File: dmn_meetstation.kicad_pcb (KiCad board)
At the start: 2 copper layers, 19.1 x 80 mm, 19 parts, among them J1 USB_OTG, J2 Conn_01x04, J3 Conn_01x15, J4 Conn_01x15, J5 Conn_01x02, U1 bh1750breakout, U2 LT1117, U3 CJMCU-8118, U4 holyiot18010

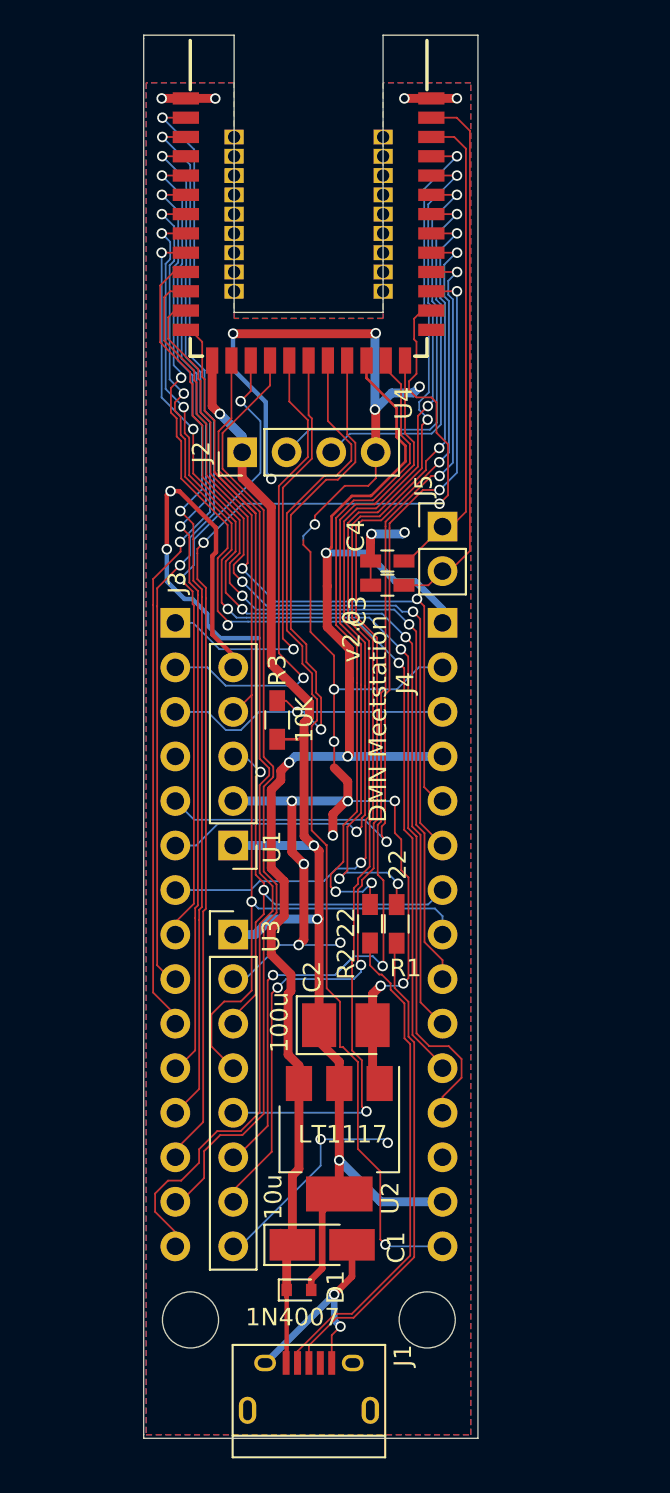
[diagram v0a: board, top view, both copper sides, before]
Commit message: Shorter pcb version
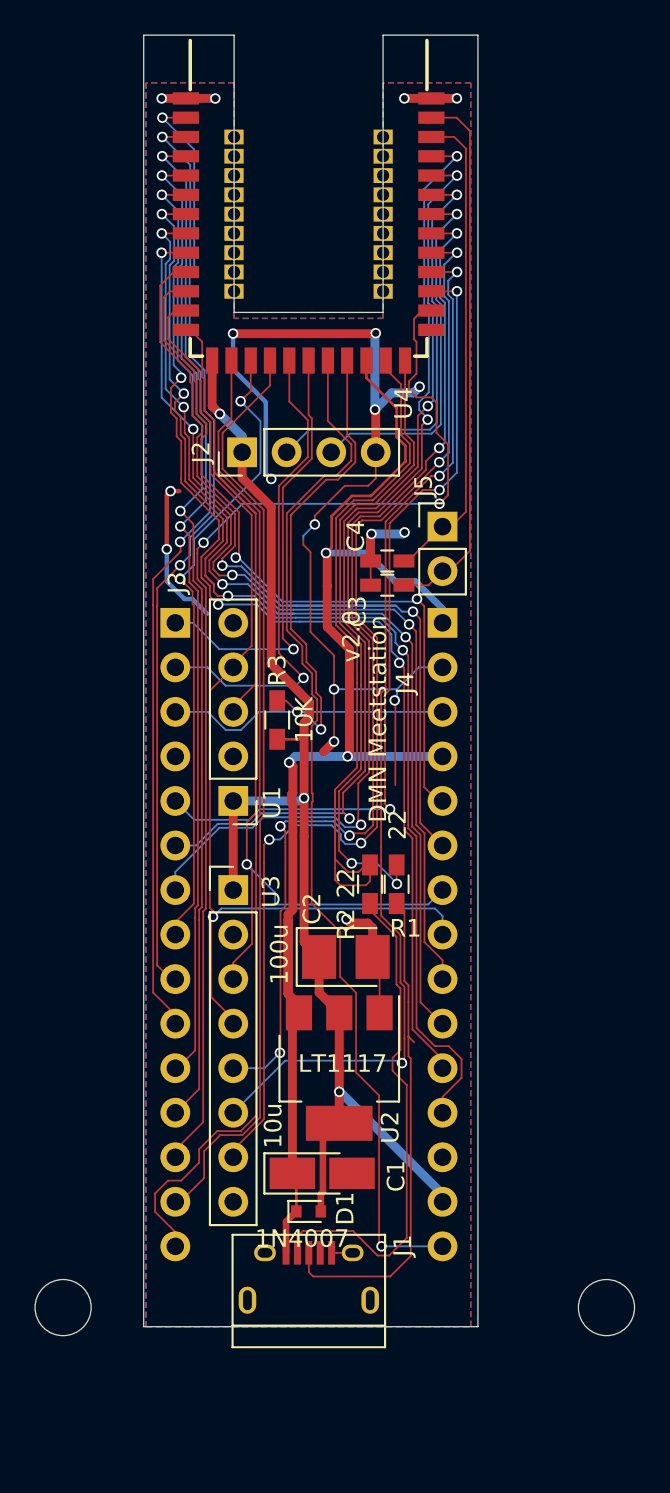
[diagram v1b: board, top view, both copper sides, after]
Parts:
- moved MH1 10.2 mm to (65.0, 141.3)
- moved MH2 7.30 mm to (34.0, 141.3)
- moved J1 6.28 mm to (48.0, 139.5)
- moved D1 4.51 mm to (48.0, 135.8)
- moved C1 4.07 mm to (48.7, 133.6)
- moved U2 4.03 mm to (49.7, 127.6)
- moved C2 3.89 mm to (50.1, 121.3)
- moved U1 2.54 mm to (43.7, 112.4)
- moved U3 2.54 mm to (43.7, 117.5)
- moved R1 2.26 mm to (53.0, 117.1)
- moved R2 2.26 mm to (51.5, 117.1)
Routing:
- net GND: track 163.7 -> 81.0 mm, vias 30 -> 17
- net (no net): track 0.00 -> 8.80 mm, vias 0 -> 2
- net /AIN6: track 45.8 -> 52.6 mm
- net /USB-: track 38.6 -> 43.4 mm, vias 2 -> 0
- net +5V: track 82.7 -> 78.3 mm
- net +3V3: track 76.0 -> 72.1 mm, vias 4 -> 3
- net /CJINT: track 63.7 -> 60.6 mm, vias 4 -> 3
- net /CJWAKE: track 64.1 -> 61.5 mm, vias 3 -> 5
- net /I2CSDA: track 62.0 -> 59.9 mm
- net /P1.00: track 48.6 -> 46.6 mm
- net /AIN0: track 66.6 -> 67.7 mm
- net /USB+: track 38.4 -> 37.4 mm
- net /SPIMOSI: track 57.3 -> 56.2 mm
- net /SPIMISO: track 54.4 -> 53.3 mm
- net /AIN4: track 58.6 -> 59.5 mm
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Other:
- board size 19.1 x 80 mm -> 19.1 x 73.7 mm

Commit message: Finalize short version layout
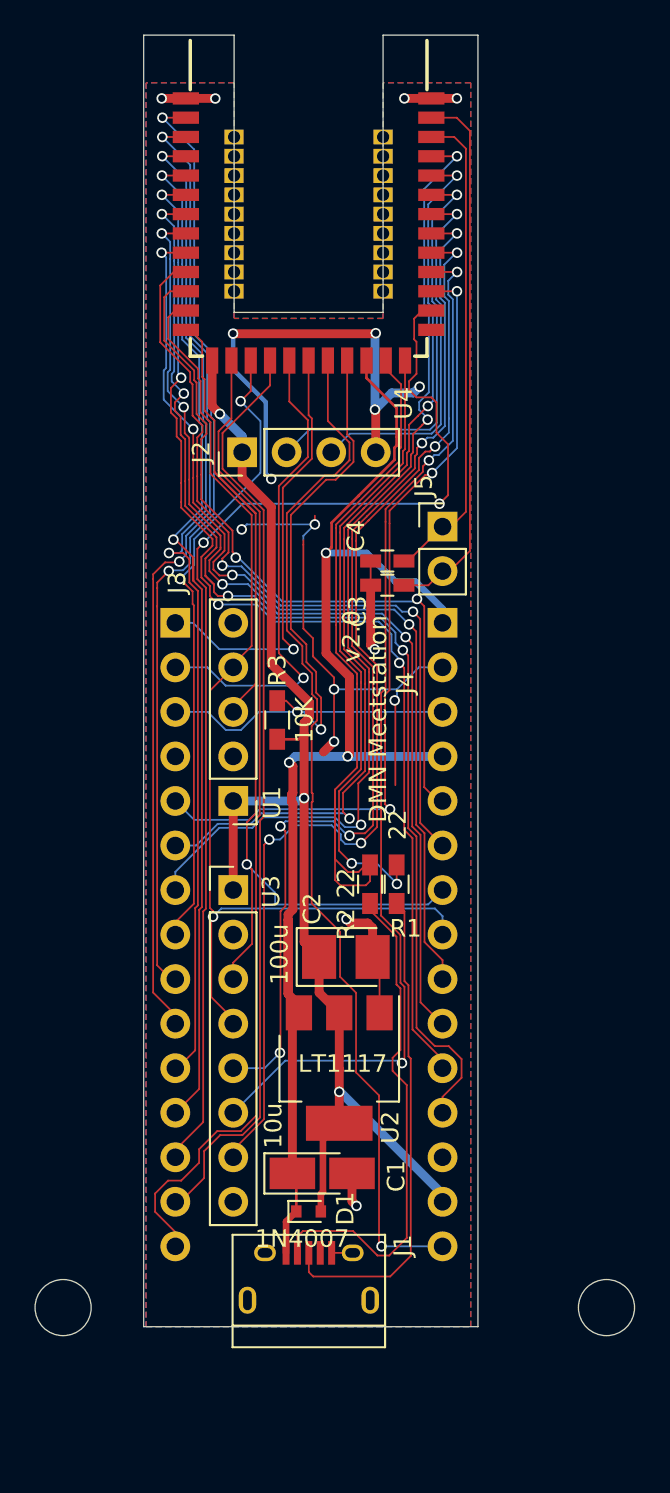
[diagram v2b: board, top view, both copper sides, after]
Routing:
- net /AIN6: track 52.6 -> 46.0 mm
- net /P1.15: track 57.9 -> 63.5 mm
- net GND: track 81.0 -> 75.7 mm, vias 17 -> 16
- net (no net): track 8.80 -> 6.03 mm
- net /P1.13: track 56.5 -> 57.6 mm
- net /AIN4: track 59.5 -> 58.3 mm
- net /USB-: track 43.4 -> 42.4 mm
- net /USB+: track 37.4 -> 36.3 mm
- net +5V: track 78.3 -> 77.2 mm
- net /P1.04: track 54.0 -> 53.3 mm
- net /P1.06: track 57.7 -> 57.0 mm
- net /AIN1: track 64.6 -> 64.0 mm
- net /CJRESET: track 64.9 -> 64.4 mm

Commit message: more compact
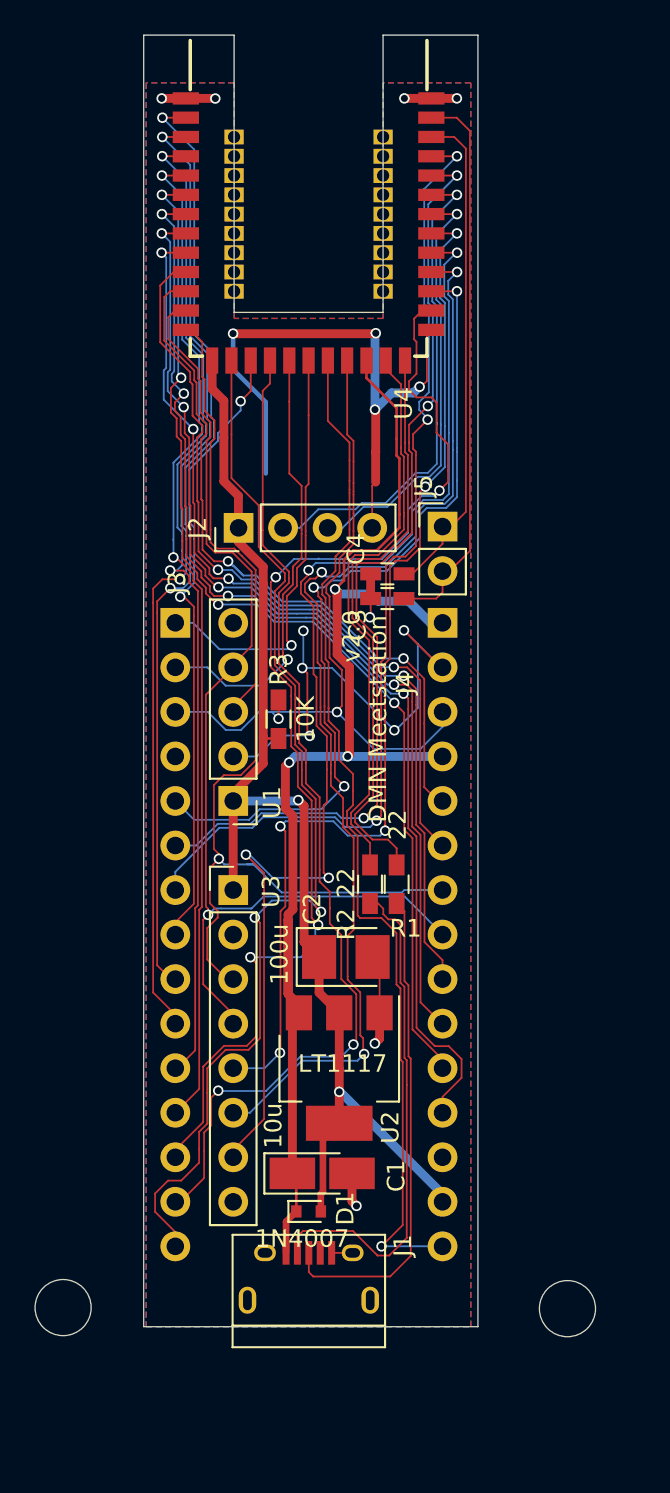
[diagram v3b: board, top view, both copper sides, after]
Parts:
- moved J2 4.32 mm to (44.0, 96.8)
- moved MH1 2.23 mm to (62.7, 141.3)
- moved C3 0.76 mm to (52.5, 100.9)
- moved C4 0.73 mm to (52.5, 99.4)
- moved R3 0.09 mm to (46.2, 107.7)
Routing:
- net /USB-: track 42.4 -> 33.2 mm
- net GND: track 75.7 -> 81.8 mm
- net (no net): track 6.03 -> 0.00 mm, vias 2 -> 0
- net /SPIMOSI: track 56.2 -> 61.8 mm, vias 0 -> 2
- net /P1.15: track 63.5 -> 58.1 mm
- net /SPIMISO: track 53.3 -> 58.6 mm, vias 0 -> 2
- net /CJRESET: track 64.4 -> 68.9 mm
- net /CJINT: track 60.5 -> 65.0 mm
- net /SWDIO: track 24.7 -> 28.1 mm
- net /SWDCLK: track 21.2 -> 24.6 mm
- net /AIN0: track 67.3 -> 64.5 mm
- net /AIN1: track 64.0 -> 61.4 mm
- net +3V3: track 72.1 -> 74.6 mm, vias 3 -> 2
- net /RX: track 28.0 -> 25.6 mm
- net /USB+: track 36.3 -> 33.9 mm, vias 2 -> 0
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
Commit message: Cleanup, more groundplane
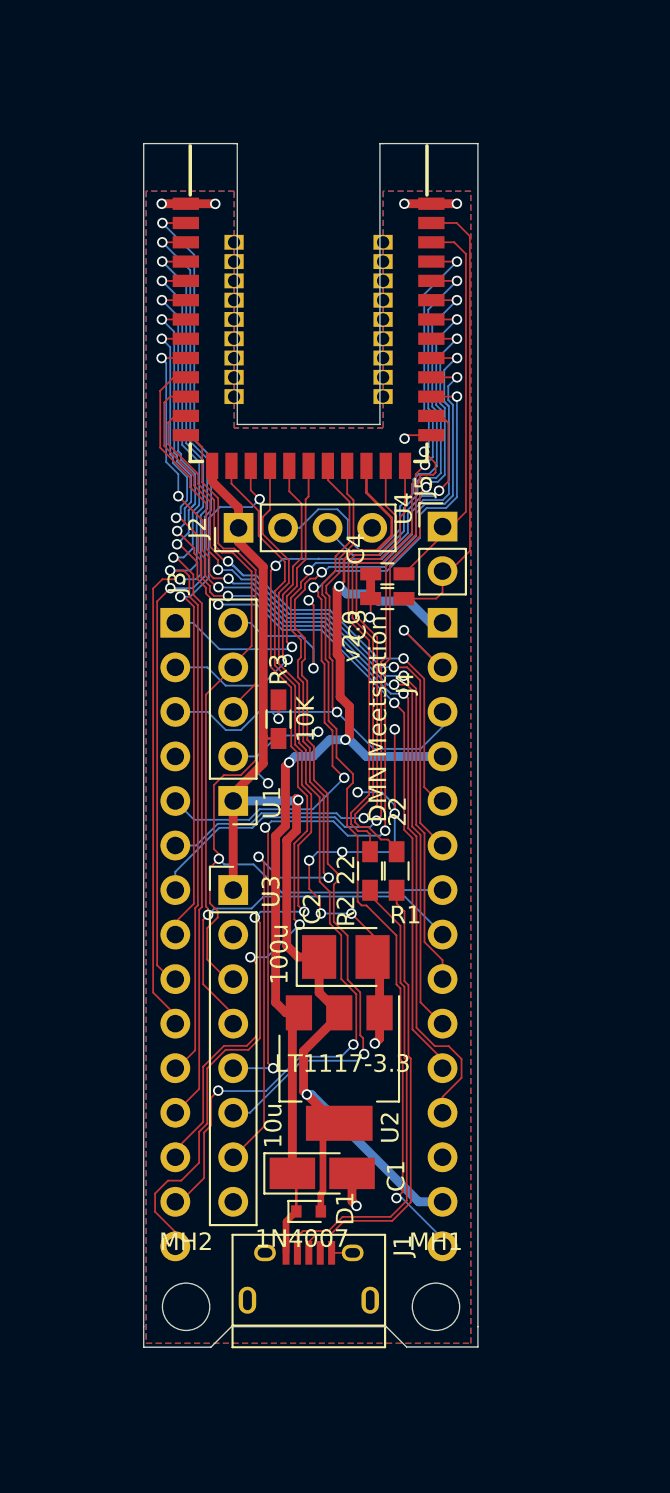
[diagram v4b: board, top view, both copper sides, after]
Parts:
- MH1, MH2: footprint Mounting_Holes:MountingHole_3.2mm_M3_DIN965 -> Mounting_Holes:MountingHole_2.7mm_M2.5
- U2: value LT1117 -> LT1117-3.3
- moved MH1 7.50 mm to (55.2, 141.2)
- moved MH2 7.01 mm to (41.0, 141.2)
- moved U4 6.01 mm to (54.7, 78.3)
- moved R1 0.75 mm to (53.0, 116.4)
- moved R2 0.75 mm to (51.5, 116.4)
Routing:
- net GND: track 81.8 -> 66.3 mm, vias 16 -> 20
- net +5V: track 76.0 -> 65.4 mm
- net /SPISCK: track 58.8 -> 49.7 mm
- net /SPICS: track 66.2 -> 58.3 mm
- net /USB+: track 33.9 -> 26.5 mm
- net /NFC1: track 29.9 -> 22.5 mm
- net /SPIMOSI: track 61.8 -> 54.5 mm
- net /USB-: track 33.2 -> 26.1 mm
- net /I2CSCL: track 58.6 -> 51.8 mm
- net /nRESET: track 42.8 -> 36.0 mm
- net /AIN7: track 41.6 -> 35.0 mm
- net /I2CSDA: track 61.7 -> 55.1 mm
- net /CJRESET: track 68.9 -> 62.3 mm
- net /AIN5: track 53.3 -> 46.8 mm
- net /AIN6: track 44.0 -> 37.7 mm
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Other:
- board size 19.1 x 73.7 mm -> 19.1 x 68.6 mm

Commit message: Cleanup
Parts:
- U2: value LT1117-3.3 -> LT1117
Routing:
- net GND: track 66.3 -> 72.6 mm, vias 20 -> 19
- net /SPIMISO: track 52.5 -> 53.8 mm
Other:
- board size 19.1 x 68.6 mm -> 19.3 x 68.6 mm
- board text added: "100"
- board text added: "104"
- board text added: "106"
- board text added: "109"
- board text added: "110"
- board text added: "111"
- board text added: "113"
- board text added: "115"
- board text added: "3V3"
- board text added: "5V"
- board text added: "A0"
- board text added: "A1"
- board text added: "A4"
- board text added: "A5"
- board text added: "A6"
- board text added: "A7"
- board text added: "CINT"
- board text added: "CRST"
- board text added: "CS"
- board text added: "GND"
- board text added: "MISO"
- board text added: "MOSI"
- board text added: "NC"
- board text added: "RST"
- board text added: "RX"
- board text added: "SCK"
- board text added: "SCL"
- board text added: "SDA"
- board text added: "SWCLK"
- board text added: "SWIO"
- board text added: "TX"
- board text added: "VCC"
- board text added: "WKE"
- board text added: "v2.1"
- board text removed: "v2.0"

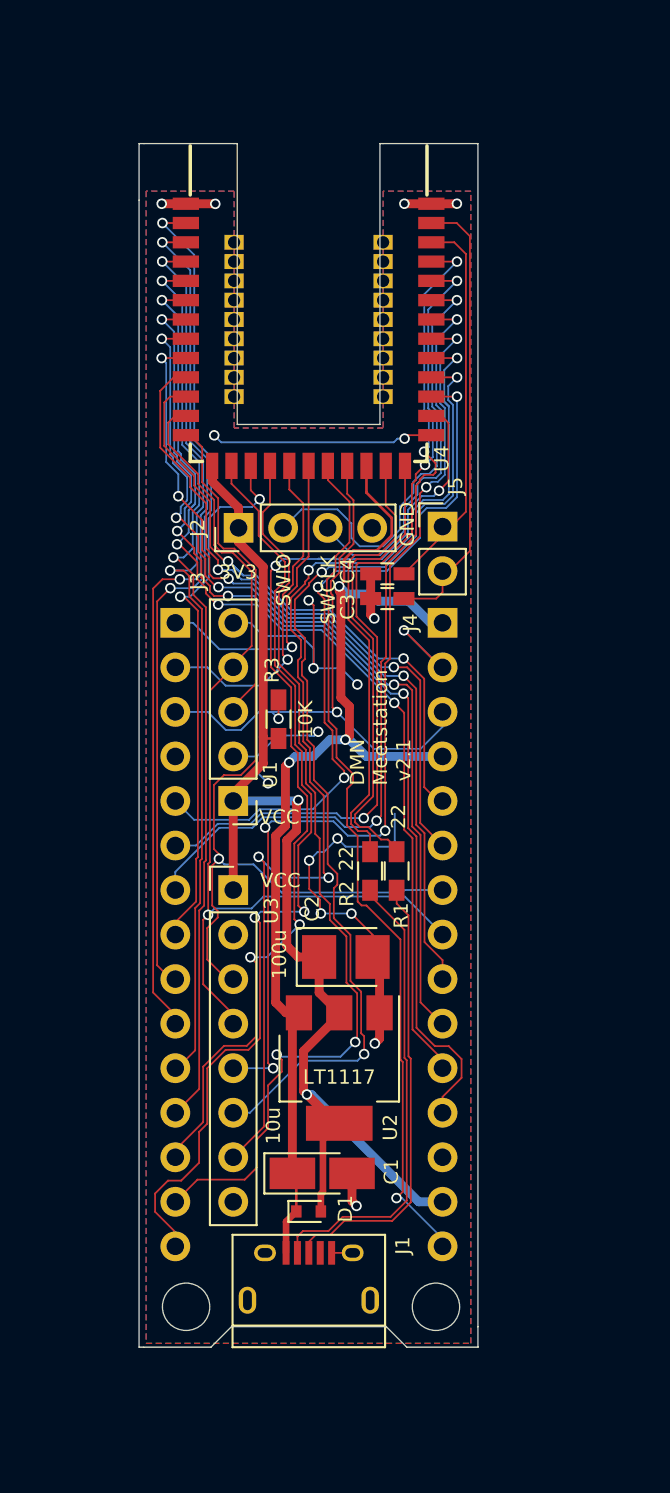
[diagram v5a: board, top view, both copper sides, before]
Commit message: Reroute to 5 mil min width
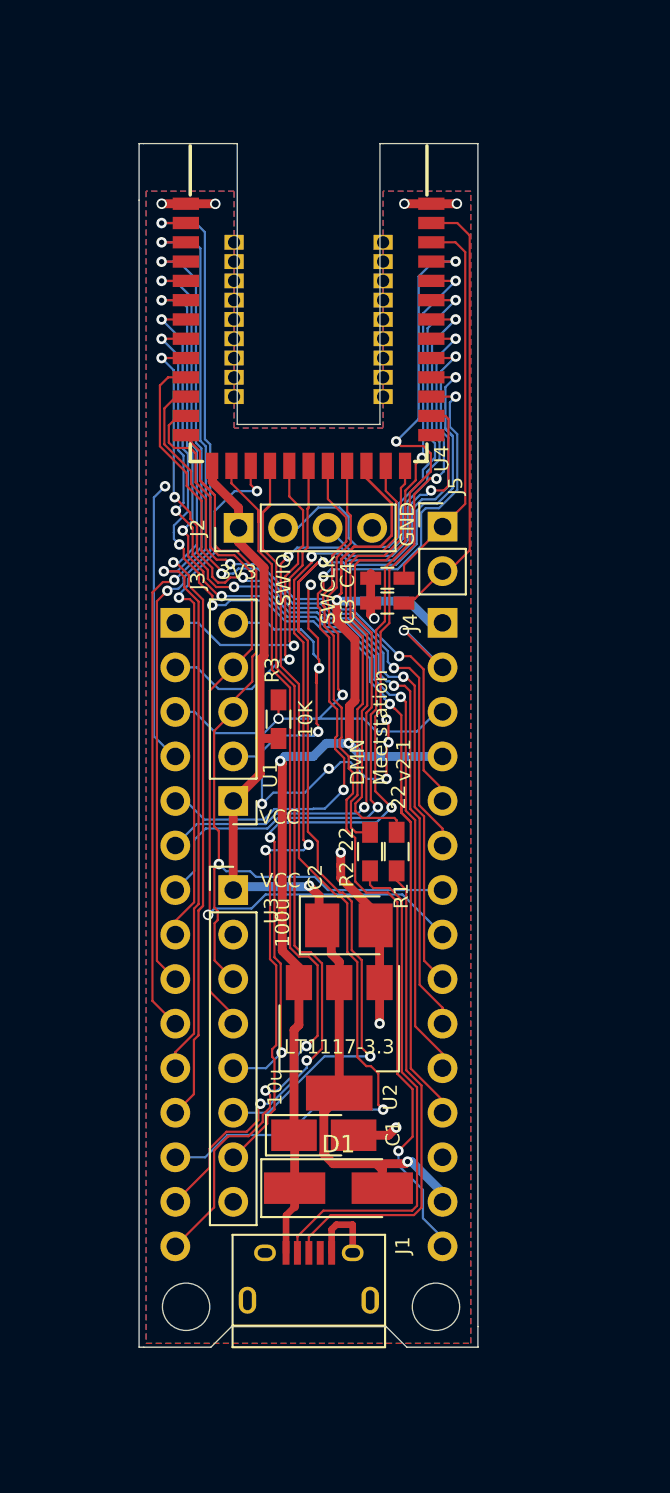
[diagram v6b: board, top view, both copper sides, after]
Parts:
- D1: footprint Diodes_SMD:D_SOD-523 -> Diodes_SMD:D_SMA_Handsoldering
- U2: value LT1117 -> LT1117-3.3
- moved C1 2.18 mm to (48.8, 131.5)
- moved D1 2.16 mm to (49.7, 134.5)
- moved C2 1.81 mm to (50.3, 119.5)
- moved U2 1.72 mm to (49.7, 125.9)
- moved R1 1.11 mm to (53.0, 115.3)
- moved R2 1.11 mm to (51.5, 115.3)
- moved C3 0.25 mm to (52.5, 101.1)
- moved C4 0.25 mm to (52.5, 99.7)
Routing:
- net GND: track 72.6 -> 90.2 mm, vias 19 -> 18
- net +3V3: track 73.1 -> 62.8 mm
- net /SPICS: track 58.3 -> 65.9 mm, vias 4 -> 3
- net /CJINT: track 59.2 -> 64.2 mm
- net Net-(J1-Pad2): track 26.6 -> 29.8 mm
- net /CJRESET: track 62.3 -> 59.3 mm
- net +5V: track 65.2 -> 68.0 mm
- net /SPIMISO: track 53.8 -> 51.1 mm
- net Net-(J1-Pad3): track 25.5 -> 27.8 mm
- net /I2CSCL: track 51.7 -> 49.6 mm
- net /SPIMOSI: track 54.5 -> 52.5 mm
- net /P1.06: track 50.7 -> 52.6 mm
- net /P1.15: track 52.5 -> 54.2 mm
- net /P1.04: track 48.3 -> 47.2 mm
- net /AIN7: track 35.0 -> 34.0 mm
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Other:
- net class Default: trace_width 0.1016 -> 0.127; via_drill 0.4 -> 0.3
- net class power: via_drill 0.4 -> 0.3
- net class wide: via_drill 0.4 -> 0.3
- rule trace_min: 0.1016 -> 0.127

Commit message: More cleanup
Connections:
- U4 pad 52: /SPIMISO -> /SPIMOSI
- U4 pad 54: /SPIMOSI -> /SPIMISO
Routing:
- net GND: track 90.2 -> 104.0 mm, vias 18 -> 20
- net /SPICS: track 65.9 -> 58.0 mm
- net /SPIMISO: track 51.1 -> 48.1 mm, vias 2 -> 0
- net +5V: track 68.0 -> 65.0 mm
- net /CJINT: track 64.2 -> 63.2 mm
- net /P1.15: track 54.2 -> 53.2 mm
- net /CJWAKE: track 55.5 -> 54.5 mm
- net /SPIMOSI: track 52.5 -> 51.9 mm, vias 2 -> 0
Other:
- board text added: "v2.2"
- board text removed: "v2.1"
